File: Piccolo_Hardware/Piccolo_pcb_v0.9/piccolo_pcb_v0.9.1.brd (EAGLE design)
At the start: 64 x 91 mm, 12 parts

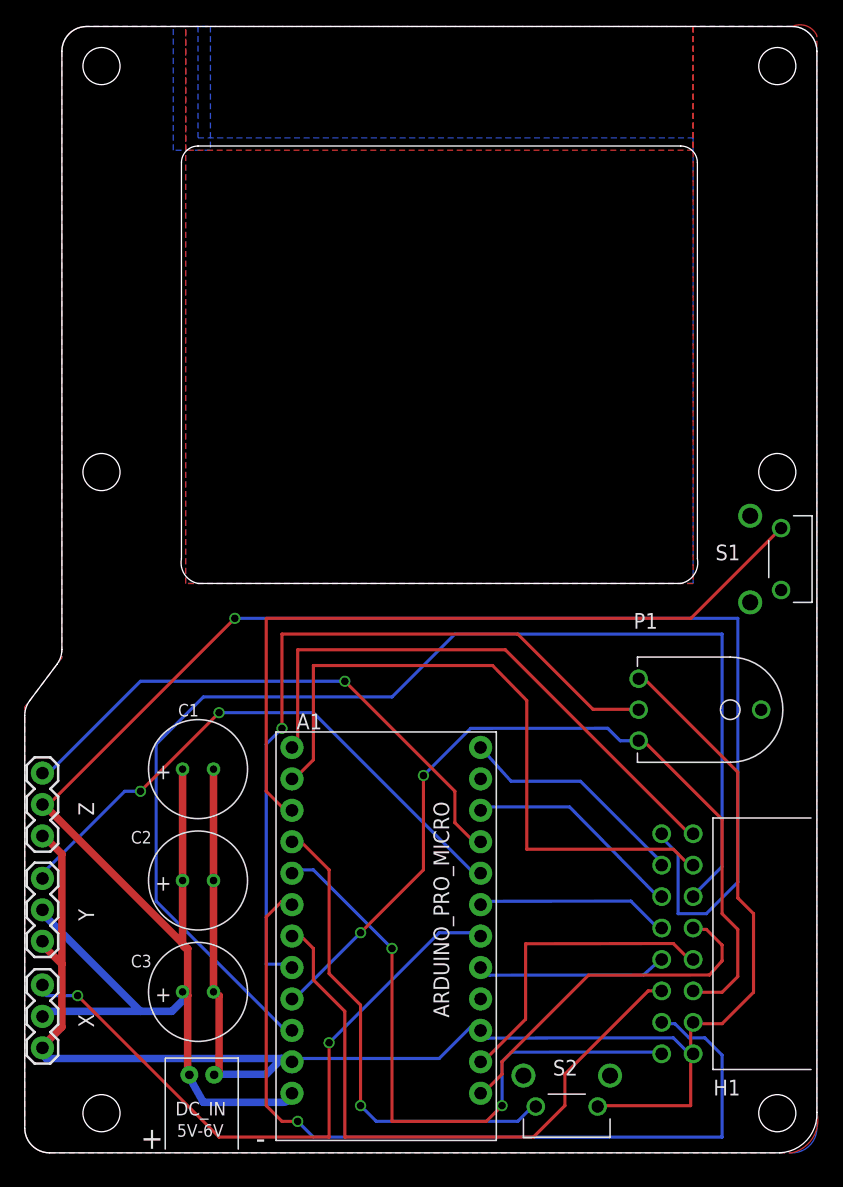
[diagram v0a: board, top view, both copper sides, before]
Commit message: Tidied piccolo pcb to make 0.10 - all traces to 16 mil or greater - removed all ground traces - removed all right angles - lots of little fixes
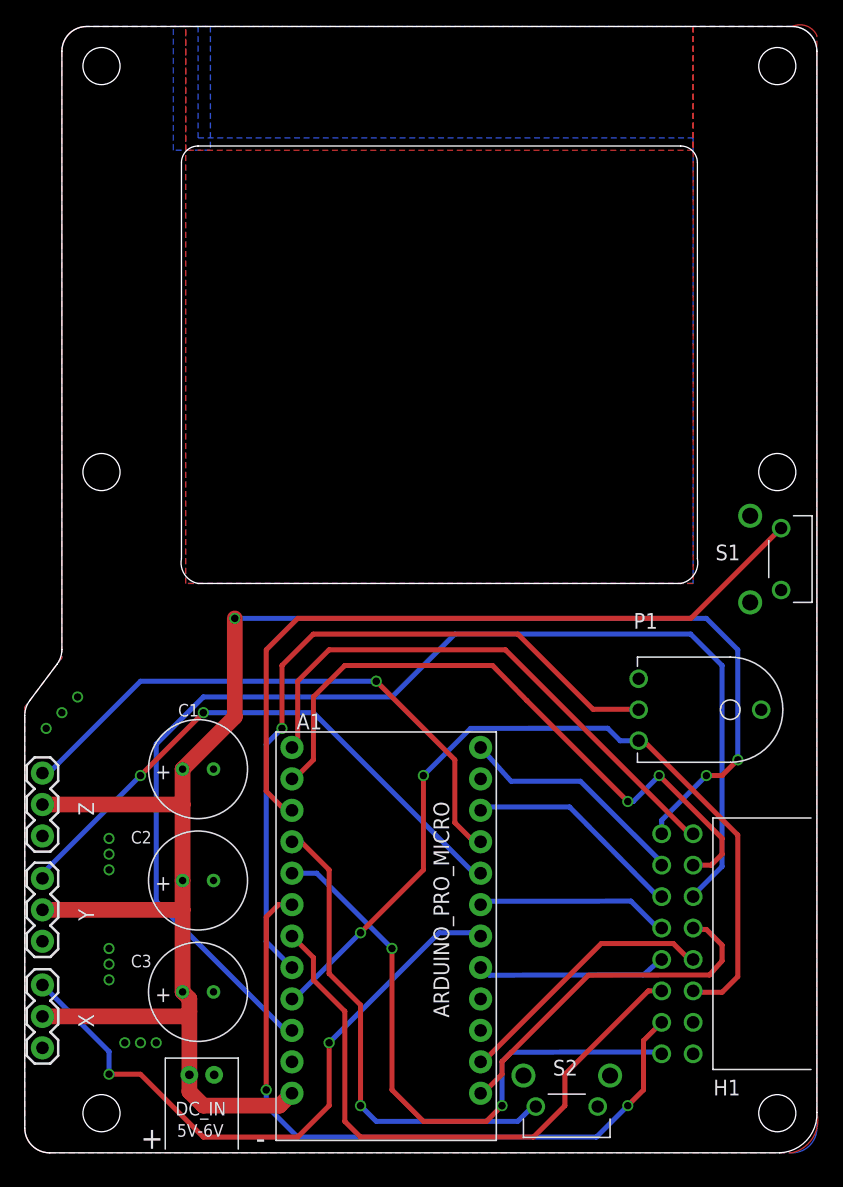
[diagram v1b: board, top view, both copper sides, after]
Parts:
- added U$1: (no value), mechanical:VHS-LOGO-SMALL
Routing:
- net GND: track 157.9 -> 0.00 mm, vias 0 -> 12
- net PWR_RAW: track 173.2 -> 144.1 mm, vias 1 -> 3
- net PIN_A1: track 68.8 -> 56.9 mm, vias 1 -> 2
- net RX: track 25.2 -> 21.6 mm
- net A3: track 61.4 -> 59.0 mm
- net PIN_A0: track 51.1 -> 49.4 mm
- net Z_PWM_PIN6: track 45.4 -> 46.9 mm
- net RESET: track 99.9 -> 98.4 mm
- net PIN10: track 46.3 -> 44.8 mm
- net N$3: track 61.2 -> 59.8 mm
- net PIN16: track 54.4 -> 53.0 mm, vias 0 -> 2
- net PIN_A2: track 50.6 -> 49.2 mm
- net X_PWM_PIN3: track 52.1 -> 51.4 mm
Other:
- board text added: "piccolo pcb v0.10"
- board text removed: "piccolo pcb v0.9"
